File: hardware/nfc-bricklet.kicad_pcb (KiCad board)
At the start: 2 copper layers, 85 x 50 mm, 47 parts, among them J1 CONN_01X03, P1 CON-SENSOR2, U1 XMC130024, U2 PN7150, U3 DRILL, U4 DRILL, U5 DRILL, U6 DRILL, U7 DRILL, U8 DRILL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

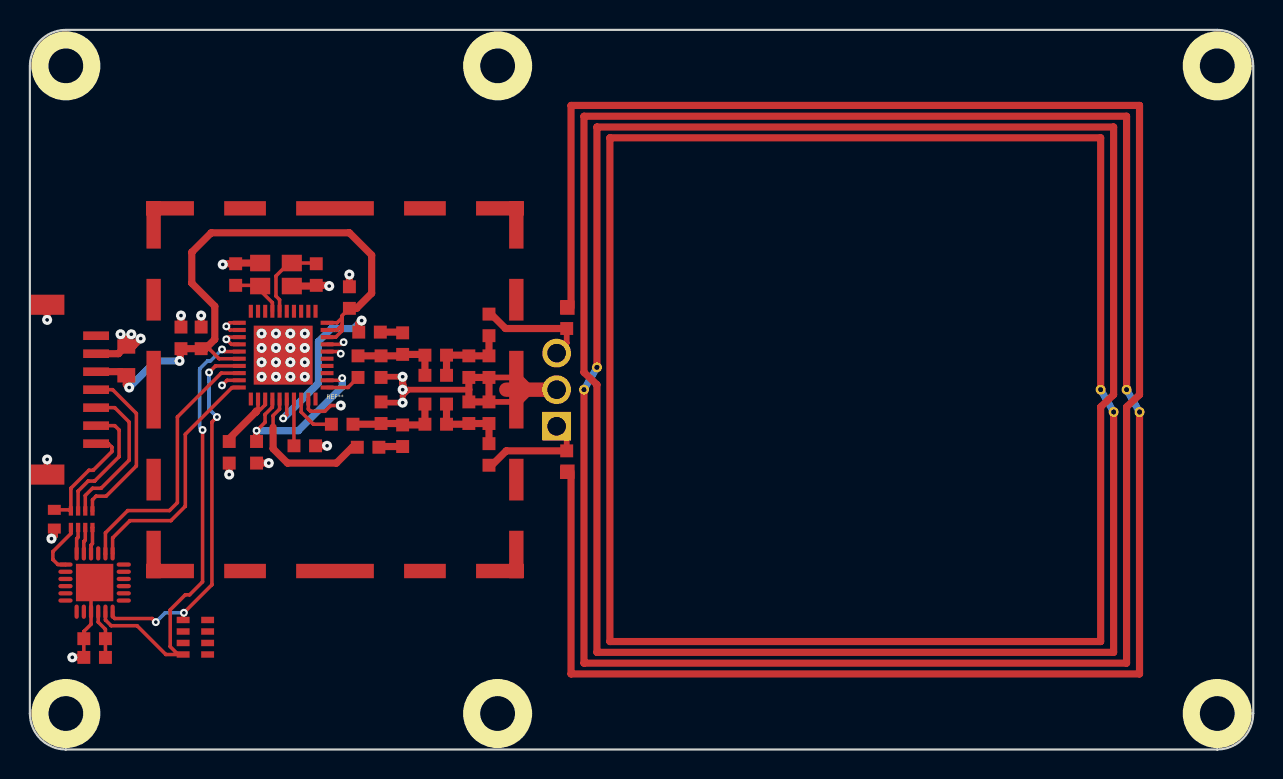
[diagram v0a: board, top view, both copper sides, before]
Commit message: fully routed
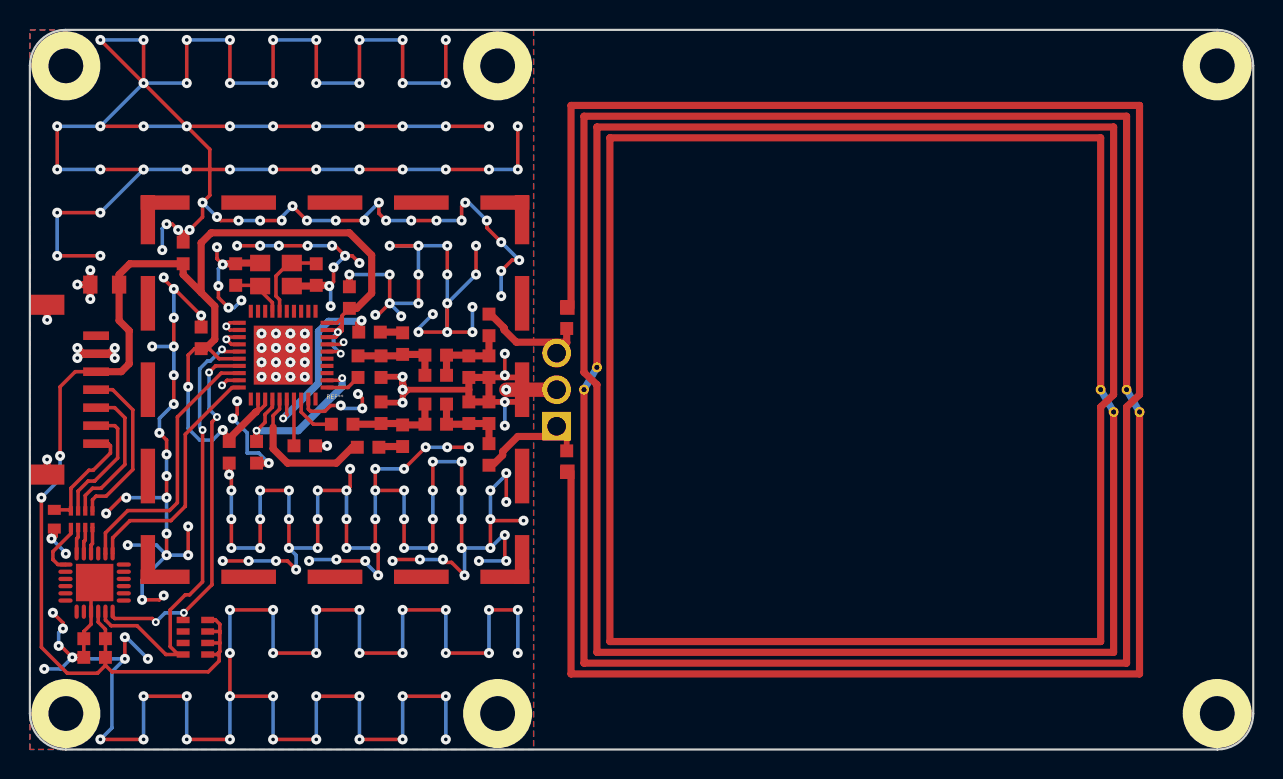
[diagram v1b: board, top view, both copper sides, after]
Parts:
- REF**: footprint kicad-libraries:WE-SHC-25X25SMD -> kicad-libraries:SHIELD-261_261
- moved C8 5.90 mm to (121.0, 67.5)
- moved C2 5.51 mm to (115.6, 69.7), turned to 180 degrees
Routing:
- net GND: track 88.2 -> 611.5 mm, vias 39 -> 268
- net VCC: track 54.2 -> 114.7 mm, vias 3 -> 6
- net Net-(J1-Pad3): track 7.91 -> 9.31 mm
- added copper zone on B.Cu, net GND
- added copper zone on F.Cu, net GND

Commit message: add logos
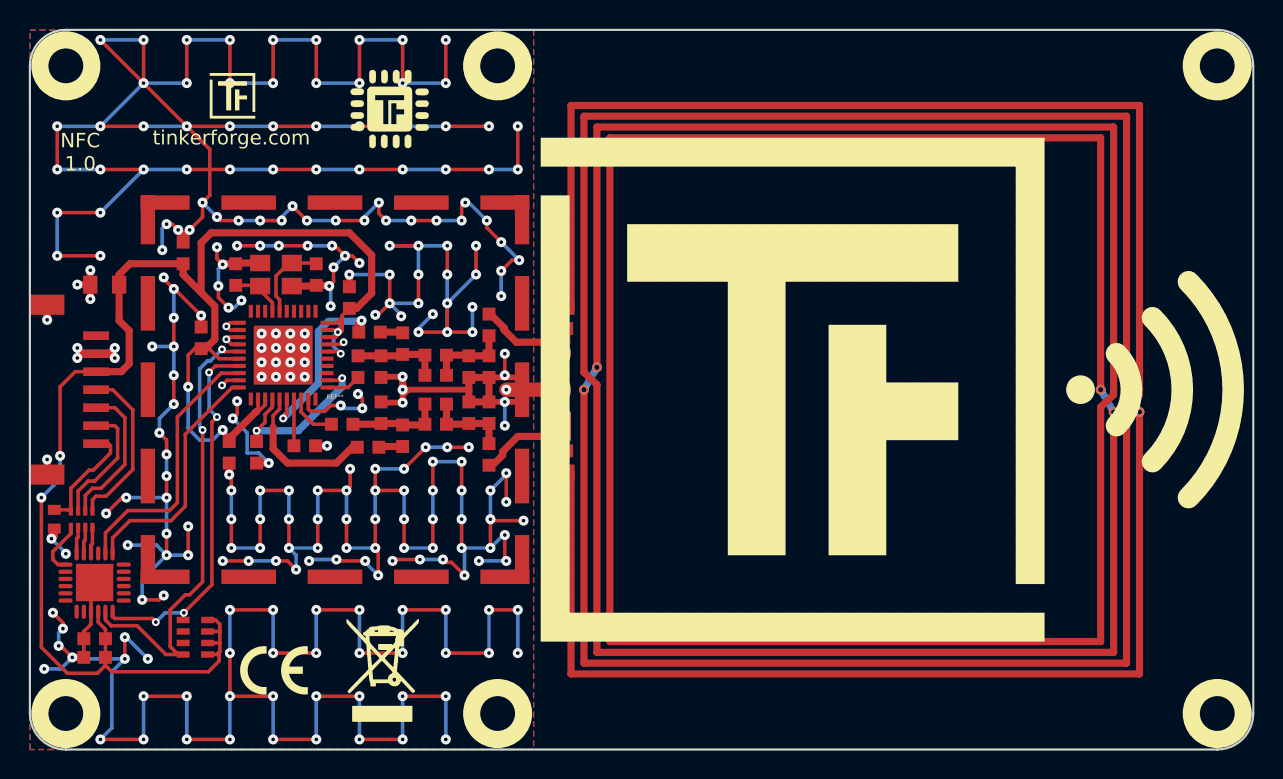
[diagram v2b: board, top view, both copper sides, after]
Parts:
- added G***: LOGO, kicad-libraries:Logo_CoMCU, F.Cu at (135.4, 57.5)
- added G***: Logo_31x31, kicad-libraries:Logo_31x31, F.Cu at (122.9, 55.0)
- added TF_ICON_35: , kicad-libraries:TF_ICON_35, F.Cu at (145.9, 59.5)
- added TF_ICON_35_FLIP: Val**, kicad-libraries:TF_ICON_35_FLIP, F.Cu at (180.9, 94.5)
- added VAL: WEEE_7mm, kicad-libraries:WEEE_7mm, F.Cu at (134.9, 96.5)
- added VAL: CE_5mm, kicad-libraries:CE_5mm, F.Cu at (127.4, 96.5)
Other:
- board text added: "NFC 1.0"
- board text added: "tinkerforge.com"

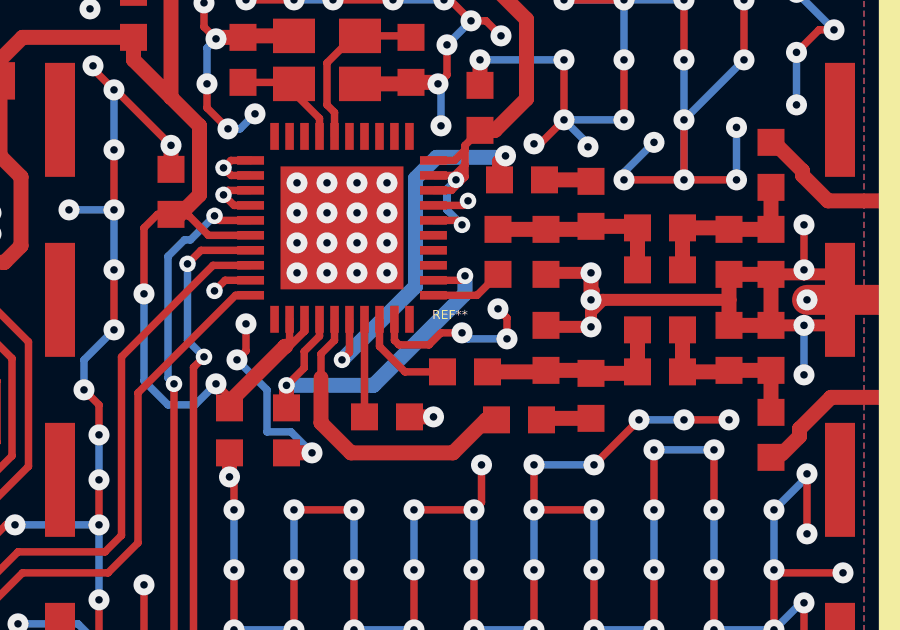
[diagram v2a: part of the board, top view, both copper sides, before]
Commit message: fix shield grounding
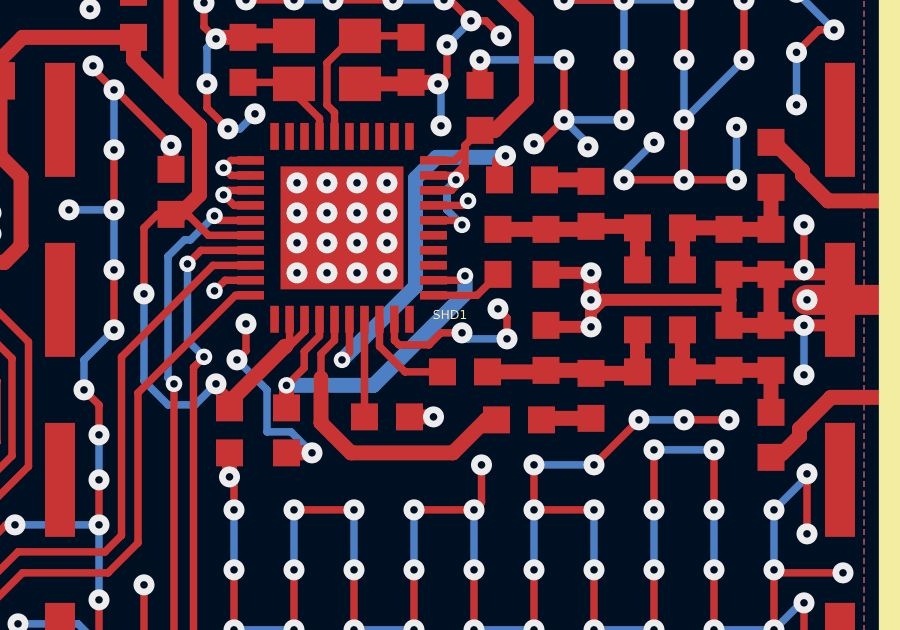
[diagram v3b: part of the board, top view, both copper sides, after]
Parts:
- removed REF**: WE-SHC-25X25SMD, kicad-libraries:SHIELD-261_261
- added SHD1: Shield, kicad-libraries:SHIELD-261_261, F.Cu at (131.6, 77.0)
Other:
- board text added: "Copyright Tinkerforge GmbH 2017. This documentation describes Open Hardware and is licensed under the CERN OHL v. 1.1. You may redistribute and modify this documentation under the terms of the CERN OHL v.1.1. (http://ohwr.org/cernohl). This documentation is distributed WITHOUT ANY EXPRESS OR IMPLIED WARRANTY, INCLUDING OF MERCHANTABILITY, SATISFACTORY QUALITY AND FITNESS FOR A PARTICULAR PURPOSE.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"
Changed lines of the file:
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@@
 (kicad_pcb (version 4) (host pcbnew 4.0.7-e2-6376~58~ubuntu17.04.1)
   (general
-    (links 105)
+    (links 125)
     (no_connects 0)
-    (area 109.494999 51.094999 196.305001 102.905001)
+    (area 110.324999 51.924999 195.475001 102.075001)
     (thickness 1.6)
-    (drawings 10)
+    (drawings 11)
     (tracks 968)
     (zones 0)
@@
   )
   (page A4)
+  (title_block
+    (title "NFC Bricklet")
+    (date 2017-09-20)
+    (rev 1.0)
+    (company "Tinkerforge GmbH")
+    (comment 1 "Licensed under CERN OHL v.1.1")
+    (comment 2 "Copyright (©) 2017, B.Nordmeyer <bastian@tinkerforge.com>")
+  )
   (layers
-    (0 F.Cu signal hide)
+    (0 F.Cu signal)
     (31 B.Cu signal hide)
     (32 B.Adhes user)
@@
       (clearance 0.89916))
   )
-  (module kicad-libraries:SHIELD-261_261 (layer F.Cu)
-    (at 131.6 77)
-    (fp_text reference REF** (at 0 0.5) (layer F.SilkS)
-      (effects (font (size 0.3 0.3) (thickness 0.075)))
-    )
-    (fp_text value WE-SHC-25X25SMD (at 0 -0.5) (layer F.Fab)
-      (effects (font (size 0.3 0.3) (thickness 0.075)))
-    )
-    (fp_line (start -13.1 -13.1) (end 13.1 -13.1) (layer F.Fab) (width 0.5))
-    (fp_line (start 13.1 -13.1) (end 13.1 13.1) (layer F.Fab) (width 0.5))
-    (fp_line (start 13.1 13.1) (end -13.1 13.1) (layer F.Fab) (width 0.5))
-    (fp_line (start -13.1 13.1) (end -13.1 -13.1) (layer F.Fab) (width 0.5))
-    (pad "" smd rect (at 13 -11.8) (size 1 3.4) (layers F.Cu F.Paste F.Mask))
-    (pad "" smd rect (at -13 -11.8) (size 1 3.4) (layers F.Cu F.Paste F.Mask))
-    (pad "" smd rect (at -13 11.8) (size 1 3.4) (layers F.Cu F.Paste F.Mask))
-    (pad "" smd rect (at 13 11.8) (size 1 3.4) (layers F.Cu F.Paste F.Mask))
-    (pad "" smd rect (at 11.8 13) (size 3.4 1) (layers F.Cu F.Paste F.Mask))
-    (pad "" smd rect (at -11.8 13) (size 3.4 1) (layers F.Cu F.Paste F.Mask))
-    (pad "" smd rect (at -11.8 -13) (size 3.4 1) (layers F.Cu F.Paste F.Mask))
-    (pad "" smd rect (at 6 13) (size 3.8 1) (layers F.Cu F.Paste F.Mask))
-    (pad "" smd rect (at -6 13) (size 3.8 1) (layers F.Cu F.Paste F.Mask))
-    (pad "" smd rect (at -6 -13) (size 3.8 1) (layers F.Cu F.Paste F.Mask))
-    (pad "" smd rect (at 6 -13) (size 3.8 1) (layers F.Cu F.Paste F.Mask))
-    (pad "" smd rect (at 0 -13) (size 3.8 1) (layers F.Cu F.Paste F.Mask))
-    (pad "" smd rect (at 0 13) (size 3.8 1) (layers F.Cu F.Paste F.Mask))
-    (pad "" smd rect (at 13 6) (size 1 3.8) (layers F.Cu F.Paste F.Mask))
-    (pad "" smd rect (at -13 6) (size 1 3.8) (layers F.Cu F.Paste F.Mask))
-    (pad "" smd rect (at -13 -6) (size 1 3.8) (layers F.Cu F.Paste F.Mask))
-    (pad "" smd rect (at -13 0) (size 1 3.8) (layers F.Cu F.Paste F.Mask))
-    (pad "" smd rect (at 13 0) (size 1 3.8) (layers F.Cu F.Paste F.Mask))
-    (pad "" smd rect (at 13 -6) (size 1 3.8) (layers F.Cu F.Paste F.Mask))
-    (pad "" smd rect (at 11.8 -13) (size 3.4 1) (layers F.Cu F.Paste F.Mask))
-  )
   (module kicad-libraries:TF_ICON_35 (layer F.Cu)
     (at 145.9 59.5)
@@
       (xy 2.3114 1.41732) (xy 2.3114 1.67132) (xy 2.3114 1.67132)) (layer F.SilkS) (width 0.00254))
   )
+  (module kicad-libraries:SHIELD-261_261 (layer F.Cu)
+    (at 131.6 77)
+    (fp_text reference SHD1 (at 0 0.5) (layer F.SilkS)
+      (effects (font (size 0.3 0.3) (thickness 0.075)))
+    )
+    (fp_text value Shield (at 0 -0.5) (layer F.Fab)
+      (effects (font (size 0.3 0.3) (thickness 0.075)))
+    )
+    (fp_line (start -13.1 -13.1) (end 13.1 -13.1) (layer F.Fab) (width 0.5))
+    (fp_line (start 13.1 -13.1) (end 13.1 13.1) (layer F.Fab) (width 0.5))
+    (fp_line (start 13.1 13.1) (end -13.1 13.1) (layer F.Fab) (width 0.5))
+    (fp_line (start -13.1 13.1) (end -13.1 -13.1) (layer F.Fab) (width 0.5))
+    (pad 1 smd rect (at 13 -11.8) (size 1 3.4) (layers F.Cu F.Paste F.Mask)
+      (net 4 GND))
+    (pad 1 smd rect (at -13 -11.8) (size 1 3.4) (layers F.Cu F.Paste F.Mask)
+      (net 4 GND))
+    (pad 1 smd rect (at -13 11.8) (size 1 3.4) (layers F.Cu F.Paste F.Mask)
+      (net 4 GND))
+    (pad 1 smd rect (at 13 11.8) (size 1 3.4) (layers F.Cu F.Paste F.Mask)
+      (net 4 GND))
+    (pad 1 smd rect (at 11.8 13) (size 3.4 1) (layers F.Cu F.Paste F.Mask)
+      (net 4 GND))
+    (pad 1 smd rect (at -11.8 13) (size 3.4 1) (layers F.Cu F.Paste F.Mask)
+      (net 4 GND))
+    (pad 1 smd rect (at -11.8 -13) (size 3.4 1) (layers F.Cu F.Paste F.Mask)
+      (net 4 GND))
+    (pad 1 smd rect (at 6 13) (size 3.8 1) (layers F.Cu F.Paste F.Mask)
+      (net 4 GND))
+    (pad 1 smd rect (at -6 13) (size 3.8 1) (layers F.Cu F.Paste F.Mask)
+      (net 4 GND))
+    (pad 1 smd rect (at -6 -13) (size 3.8 1) (layers F.Cu F.Paste F.Mask)
+      (net 4 GND))
+    (pad 1 smd rect (at 6 -13) (size 3.8 1) (layers F.Cu F.Paste F.Mask)
+      (net 4 GND))
+    (pad 1 smd rect (at 0 -13) (size 3.8 1) (layers F.Cu F.Paste F.Mask)
+      (net 4 GND))
+    (pad 1 smd rect (at 0 13) (size 3.8 1) (layers F.Cu F.Paste F.Mask)
+      (net 4 GND))
+    (pad 1 smd rect (at 13 6) (size 1 3.8) (layers F.Cu F.Paste F.Mask)
+      (net 4 GND))
+    (pad 1 smd rect (at -13 6) (size 1 3.8) (layers F.Cu F.Paste F.Mask)
+      (net 4 GND))
+    (pad 1 smd rect (at -13 -6) (size 1 3.8) (layers F.Cu F.Paste F.Mask)
+      (net 4 GND))
+    (pad 1 smd rect (at -13 0) (size 1 3.8) (layers F.Cu F.Paste F.Mask)
+      (net 4 GND))
+    (pad 1 smd rect (at 13 0) (size 1 3.8) (layers F.Cu F.Paste F.Mask)
+      (net 4 GND))
+    (pad 1 smd rect (at 13 -6) (size 1 3.8) (layers F.Cu F.Paste F.Mask)
+      (net 4 GND))
+    (pad 1 smd rect (at 11.8 -13) (size 3.4 1) (layers F.Cu F.Paste F.Mask)
+      (net 4 GND))
+  )
+  (gr_text "Copyright Tinkerforge GmbH 2017.\nThis documentation describes Open Hardware and is licensed under the\nCERN OHL v. 1.1.\nYou may redistribute and modify this documentation under the terms of the\nCERN OHL v.1.1. (http://ohwr.org/cernohl). This documentation is distributed\nWITHOUT ANY EXPRESS OR IMPLIED WARRANTY, INCLUDING OF\nMERCHANTABILITY, SATISFACTORY QUALITY AND FITNESS FOR A\nPARTICULAR PURPOSE. Please see the CERN OHL v.1.1 for applicable\nconditions" (at 231 149.7) (layer Cmts.User)
+    (effects (font (size 1.5 1.5) (thickness 0.3)))
+  )
   (gr_text tinkerforge.com (at 124.4 59.5) (layer F.SilkS)
     (effects (font (size 1 1) (thickness 0.15)))
@@
   (via (at 136.3 77.9) (size 0.7) (drill 0.25) (layers F.Cu B.Cu) (net 4))
   (segment (start 142.3 76.15) (end 143.4 76.15) (width 0.4) (layer F.Cu) (net 4))
-  (segment (start 143.4 76.15) (end 144.45 76.15) (width 0.4) (layer F.Cu) (net 4))
-  (segment (start 144.45 76.15) (end 145.3 77) (width 0.4) (layer F.Cu) (net 4))
   (segment (start 142.3 77.85) (end 143.4 77.85) (width 0.4) (layer F.Cu) (net 4))
-  (segment (start 143.4 77.85) (end 144.45 77.85) (width 0.4) (layer F.Cu) (net 4))
-  (segment (start 144.45 77.85) (end 145.3 77) (width 0.4) (layer F.Cu) (net 4))
   (segment (start 145.3 77) (end 147 77) (width 0.4) (layer F.Cu) (net 4))
   (segment (start 134.8 76.15) (end 134.85 76.1) (width 0.4) (layer F.Cu) (net 4))
@@
   (segment (start 142.3 76.15) (end 140.9 76.15) (width 0.5) (layer F.Cu) (net 4))
   (segment (start 142.3 77.85) (end 142.3 76.15) (width 0.5) (layer F.Cu) (net 4))
+  (segment (start 143.4 76.15) (end 144.45 76.15) (width 0.4) (layer F.Cu) (net 4))
+  (segment (start 144.45 76.15) (end 145.3 77) (width 0.4) (layer F.Cu) (net 4))
+  (segment (start 143.4 77.85) (end 144.45 77.85) (width 0.4) (layer F.Cu) (net 4))
+  (segment (start 144.45 77.85) (end 145.3 77) (width 0.4) (layer F.Cu) (net 4))
   (segment (start 132 74.5) (end 131.5 74) (width 0.25) (layer B.Cu) (net 5))
   (segment (start 131.85108 74.35108) (end 132 74.5) (width 0.25) (layer F.Cu) (net 5))
@@
     (connect_pads (clearance 0.15))
     (min_thickness 0.15)
-    (fill yes (arc_segments 16) (thermal_gap 0.508) (thermal_bridge_width 0.508))
+    (fill yes (arc_segments 16) (thermal_gap 0.2) (thermal_bridge_width 0.25))
     (polygon
       (pts
